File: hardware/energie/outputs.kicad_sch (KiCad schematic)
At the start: 39 parts, among them J5 pilotes, U10 VOM160NT, U11 VOM160NT, U12 VOM160NT, U13 VOM160NT, U14 VOM160NT, U15 VOM160NT, U6 VOM160NT, U7 VOM160NT, U8 VOM160NT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

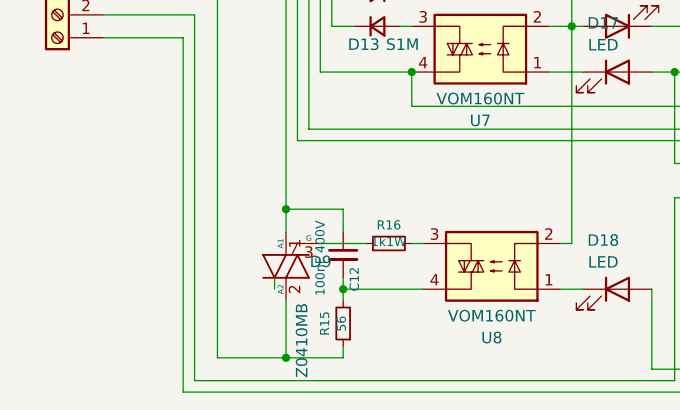
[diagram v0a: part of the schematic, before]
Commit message: Remplace le MCP6006 par MCP6007 que l'on a en stock
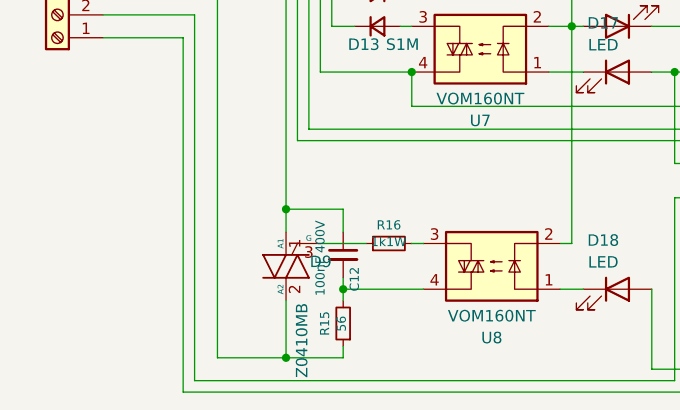
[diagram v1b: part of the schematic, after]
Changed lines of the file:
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@@
-	(wire
-		(pts
-			(xy 85.09 111.76) (xy 85.09 113.03)
-		)
-		(stroke
-			(width 0)
-			(type default)
-		)
-	)
 	(wire
 		(pts

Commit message: Adjust some references and availability
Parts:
- C12, C13: P/N C1808X104KBRAC -> C1808V104KBRACTU
- D14, D15, D16, D17, D18, D24, D25, D26, D27, D28: P/N APT1608EC -> APT1608EC (stock)
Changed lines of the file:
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@@
 			)
 		)
-		(property "P/N" "C1808X104KBRAC"
+		(property "P/N" " C1808V104KBRACTU "
 			(at 160.02 109.22 90)
 			(effects
@@
 			)
 		)
-		(property "P/N" "APT1608EC"
+		(property "P/N" "APT1608EC (stock)"
 			(at 123.19 55.88 0)
 			(effects
@@
 			)
 		)
-		(property "P/N" "APT1608EC"
+		(property "P/N" "APT1608EC (stock)"
 			(at 190.5 83.82 0)
 			(effects
@@
 			)
 		)
-		(property "P/N" "APT1608EC"
+		(property "P/N" "APT1608EC (stock)"
 			(at 190.5 88.9 0)
 			(effects
@@
 			)
 		)
-		(property "P/N" "APT1608EC"
+		(property "P/N" "APT1608EC (stock)"
 			(at 123.19 60.96 0)
 			(effects
@@
 			)
 		)
-		(property "P/N" "APT1608EC"
+		(property "P/N" "APT1608EC (stock)"
 			(at 123.19 83.82 0)
 			(effects
@@
 			)
 		)
-		(property "P/N" "C1808X104KBRAC"
+		(property "P/N" " C1808V104KBRACTU "
 			(at 92.71 109.22 90)
 			(effects
@@
 			)
 		)
-		(property "P/N" "APT1608EC"
+		(property "P/N" "APT1608EC (stock)"
 			(at 123.19 88.9 0)
 			(effects
@@
 			)
 		)
-		(property "P/N" "APT1608EC"
+		(property "P/N" "APT1608EC (stock)"
 			(at 190.5 113.03 0)
 			(effects
@@
 			)
 		)
-		(property "P/N" "APT1608EC"
+		(property "P/N" "APT1608EC (stock)"
 			(at 190.5 55.88 0)
 			(effects
@@
 			)
 		)
-		(property "P/N" "APT1608EC"
+		(property "P/N" "APT1608EC (stock)"
 			(at 123.19 113.03 0)
 			(effects
@@
 			)
 		)
-		(property "P/N" "APT1608EC"
+		(property "P/N" "APT1608EC (stock)"
 			(at 190.5 60.96 0)
 			(effects

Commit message: Fix Q2 wiring, it was reversed Fix U5 footprint Fix C10 and similar footprints
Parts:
- C12, C13: footprint Capacitor_SMD:C_1812_4532Metric -> local:C_1808_4520Metric_Pad1.72x2.30mm_HandSolder
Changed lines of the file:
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@@
 			)
 		)
-		(property "Footprint" "Capacitor_SMD:C_1812_4532Metric"
+		(property "Footprint" "local:C_1808_4520Metric_Pad1.72x2.30mm_HandSolder"
 			(at 160.9852 113.03 0)
 			(effects
@@
 			)
 		)
-		(property "Footprint" "Capacitor_SMD:C_1812_4532Metric"
+		(property "Footprint" "local:C_1808_4520Metric_Pad1.72x2.30mm_HandSolder"
 			(at 93.6752 113.03 0)
 			(effects
